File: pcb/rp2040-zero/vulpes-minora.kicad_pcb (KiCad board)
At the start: 2 copper layers, 124.6 x 95.7 mm, 60 parts, among them J13 Conn_01x04_Female, J2 AudioJack4dpb, J3 AudioJack4dpb, SW10 SW_Push, SW11 SW_Push, SW12 SW_Push, SW14 SW_Push, SW15 SW_Push, SW16 SW_Push, SW17 SW_Push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

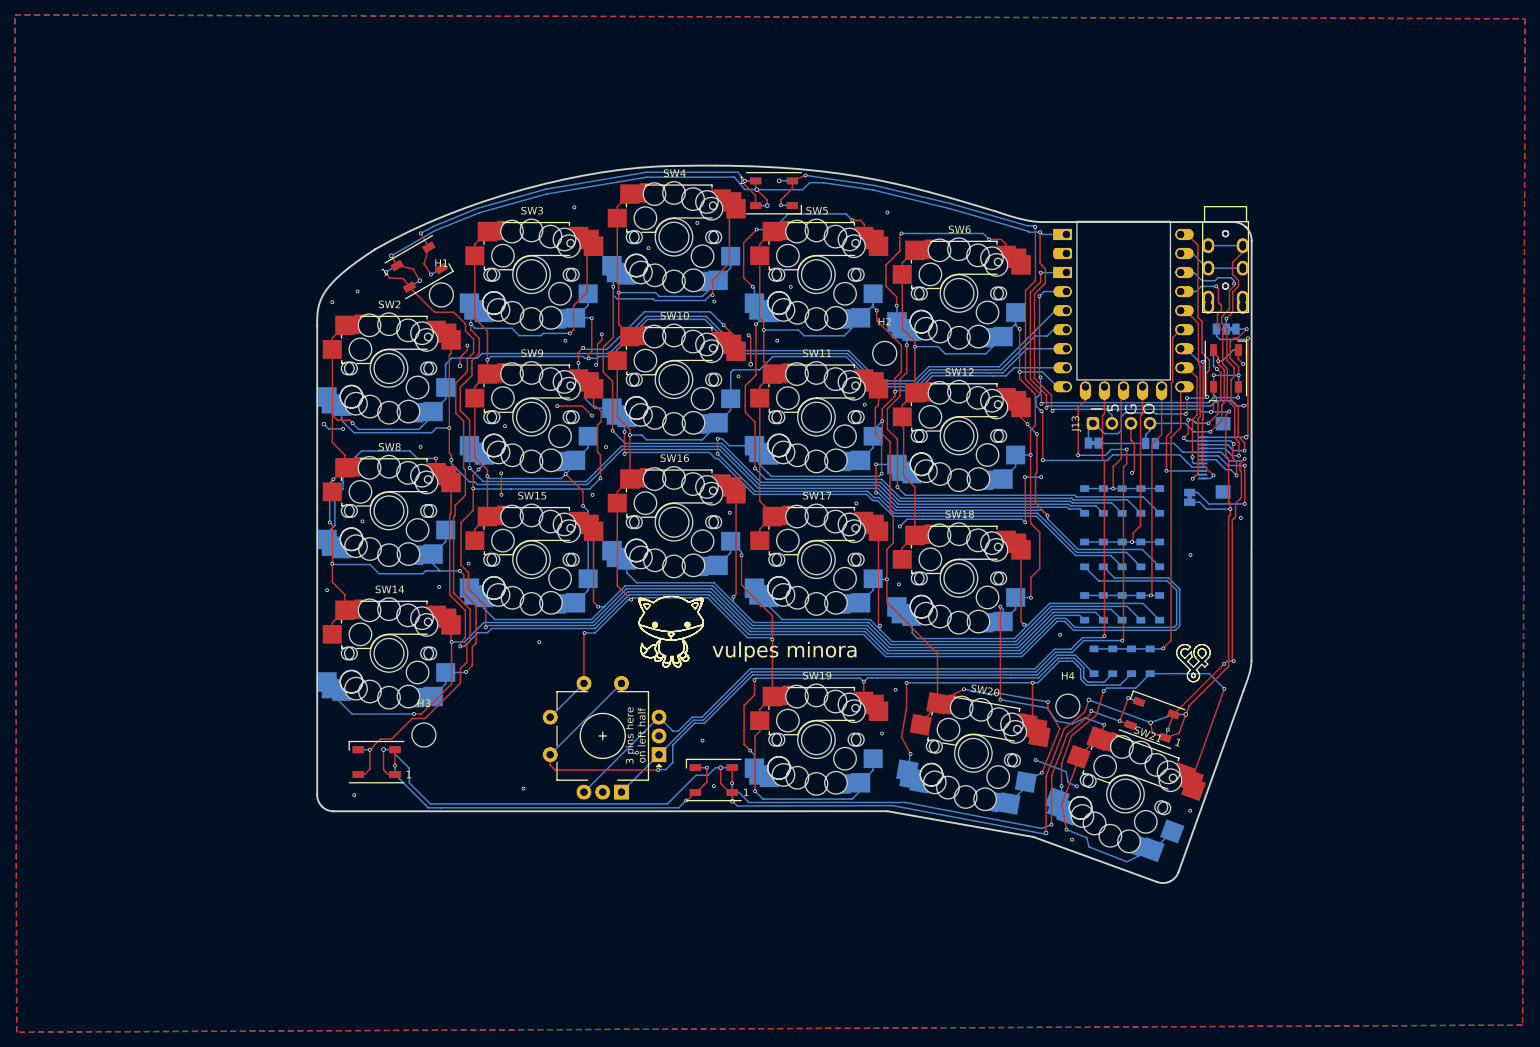
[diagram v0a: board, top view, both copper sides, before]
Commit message: fixed reversible 3 switch type footprints and regenerated gerbers
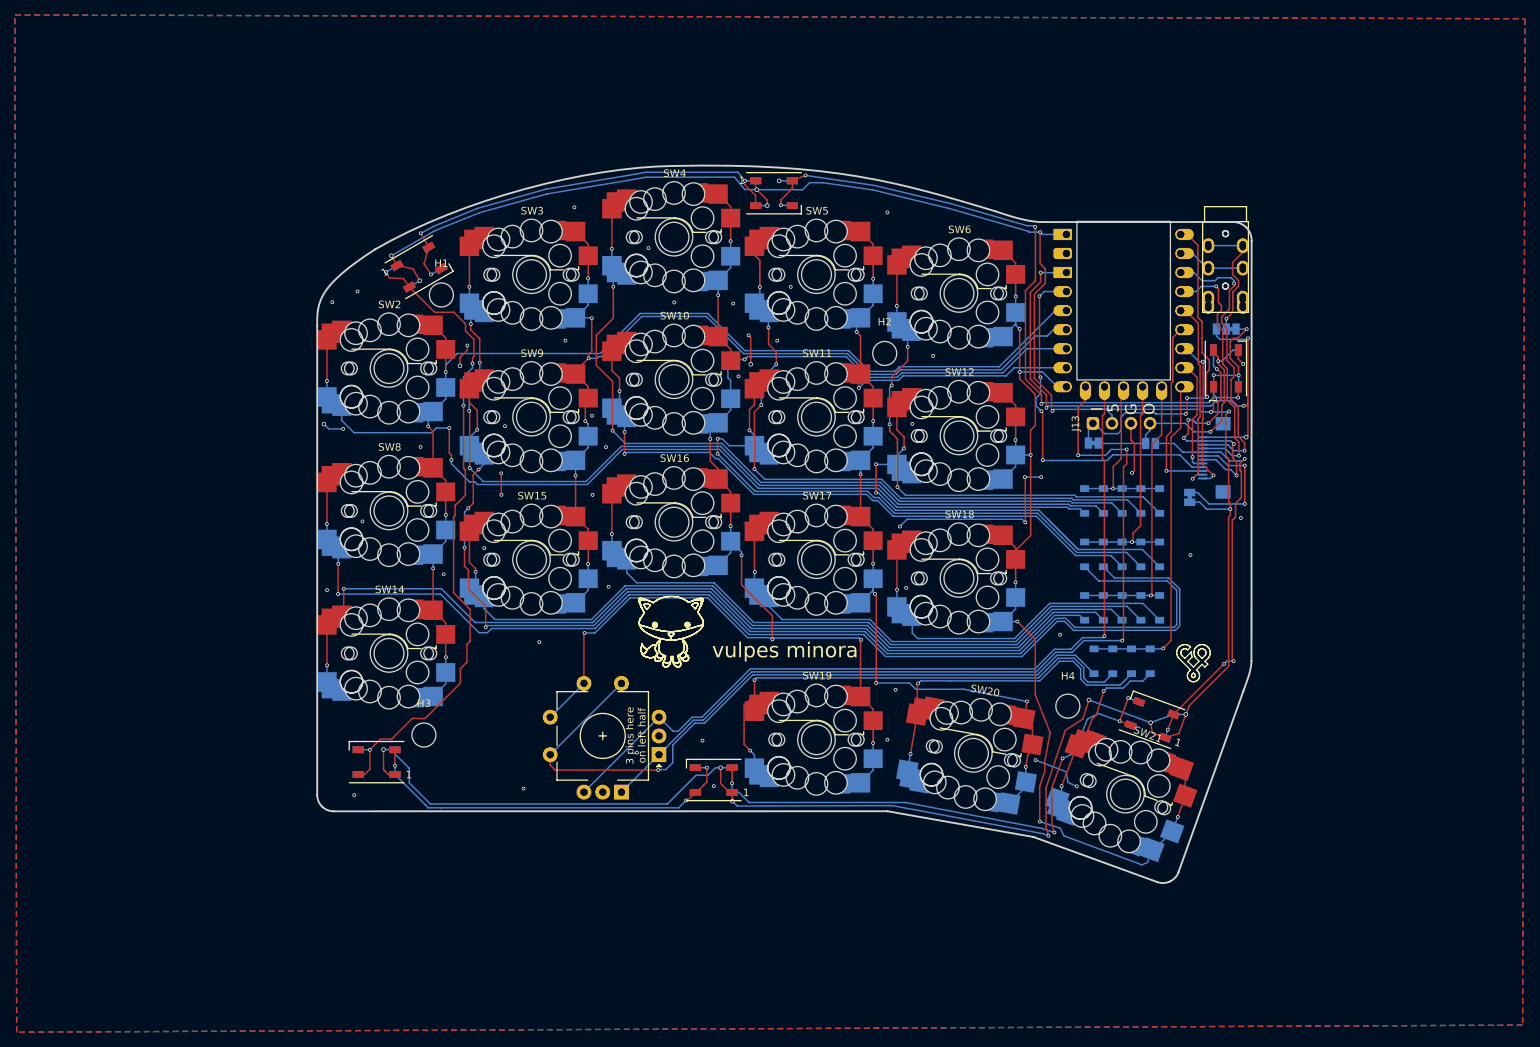
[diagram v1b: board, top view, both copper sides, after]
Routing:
- net col3: track 198.3 -> 136.7 mm, vias 8 -> 10
- net col0: track 207.9 -> 147.4 mm, vias 6 -> 5
- net col2: track 249.4 -> 194.5 mm, vias 7 -> 10
- net col1: track 178.7 -> 128.8 mm
- net col4: track 182.1 -> 141.8 mm
- net Net-(D10-A): track 115.0 -> 86.1 mm, vias 5 -> 3
- net Net-(D21-A): track 47.5 -> 22.2 mm, vias 3 -> 2
- net Net-(D11-A): track 100.6 -> 78.1 mm
- net Net-(D9-A): track 174.3 -> 151.9 mm, vias 4 -> 5
- net Net-(D6-A): track 88.8 -> 67.4 mm
- net Net-(D5-A): track 104.9 -> 84.6 mm
- net Net-(D3-A): track 141.1 -> 120.8 mm, vias 3 -> 5
- net Net-(D4-A): track 122.6 -> 103.2 mm
- net Net-(D8-A): track 171.2 -> 152.7 mm, vias 2 -> 3
- net GND: track 99.3 -> 89.8 mm, vias 63 -> 58
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
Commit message: updated vulpes minora to match new vik standard of two gpio, corresponding to commit 57a4fb79db6f66c8cfaf2971141367c47d66a44f in the vik repo
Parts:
- removed D98: 1N4148W, Diode_SMD:D_SOD-123
- removed SW47, SW48: RotaryEncoder_Switch, fingerpunch:RotaryEncoder_EC11-no-legs
- added BZ1: Buzzer, fingerpunch:AST1109MLTRQ, F.Cu at (234.5, 133.9)
- added BZ2: Buzzer, fingerpunch:AST1109MLTRQ, B.Cu at (234.5, 133.9)
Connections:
- J4 pad 7: GND -> GPIO_X1
- J4 pad 9: GPIO_X1 -> GPIO_X2
- U4 pad 13: ENC_B -> AUDIO
- U4 pad 14: ENC_A -> GPIO_X1
- U4 pad 20: GPIO_X1 -> GPIO_X2
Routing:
- net ENC_A: track 117.2 -> 0.00 mm, vias 3 -> 0
- net ENC_B: track 113.0 -> 0.00 mm, vias 1 -> 0
- net Net-(D98-A): track 96.3 -> 0.00 mm, vias 1 -> 0
- net AUDIO: track 0.00 -> 50.5 mm, vias 0 -> 2
- net GPIO_X2: track 0.00 -> 48.1 mm, vias 0 -> 4
- net col2: track 194.5 -> 152.1 mm, vias 10 -> 9
- net GPIO_X1: track 48.7 -> 27.0 mm, vias 4 -> 1
- net GND: track 89.8 -> 84.4 mm, vias 58 -> 57
- net row3: track 45.1 -> 42.6 mm
- net MOSI: track 15.7 -> 18.0 mm
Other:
- board text removed: "3 pins here on left half"
- board text removed: "3 pins here on right half"
